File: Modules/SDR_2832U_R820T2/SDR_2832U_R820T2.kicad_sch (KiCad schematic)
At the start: 0 parts

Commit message: RTL Module Schematic
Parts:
- added C1, C2: 1u, libraries:Worthington_C_0402, symbol Device:C_Small
- added C10, C11, C12, C13, C14, C15, C16, C17, C18, C19, C20, C21, C22, C23, C24, C25, C26, C29, C30, C31, C32, C33, C52, C54, C55, C56, C57, C58, C59, C60, C63, C64, C7, C8, C9: 100n, libraries:Worthington_C_0201, symbol Device:C_Small
- added C27, C4, C5, C6, C62: 10u, libraries:Worthington_C_0402, symbol Device:C_Small
- added C28: 47u, libraries:Worthington_C_0805, symbol Device:C_Small
- added C34: 1n, ±10%, Capacitor_SMD:C_1808_4520Metric, symbol Device:C_Small
- added C37: 2u2, libraries:Worthington_C_0402_0603, symbol Device:C_Small
- added C50: 6n8, libraries:Worthington_C_0201, symbol Device:C_Small
- added C53: 330p, libraries:Worthington_C_0201, symbol Device:C_Small
- added C61: 1u, libraries:Worthington_C_0201, symbol Device:C_Small
- added D1: SM05CN-SL, Package_TO_SOT_SMD:SOT-23, symbol Power_Protection:NUP2105L
- added D10, D11, D12, D13, D9: SLZST311N10, Diode_SMD:D_SOD-882, symbol Diode:ESD9B3.3ST5G
- added D14: RB521S-30, Diode_SMD:D_SOD-523, symbol Device:D_Schottky
- added D6: RED, libraries:Worthington_LED_0402, symbol Device:LED_Filled
- added DN1: D3V3X8U9LP3810, Package_DFN_QFN:Diodes_UDFN3810-9_TYPE_B, symbol Power_Protection:D3V3X8U9LP3810
- added H1, H2, H3, H4: M2.5, MountingHole:MountingHole_2.7mm_M2.5_ISO7380_Pad, symbol Mechanical:MountingHole_Pad
- added J1: USB_C_Receptacle_USB2.0_16P, symbol Connector:USB_C_Receptacle_USB2.0_16P
- added J10, J11, J12, J8, J9: SMA, Connector_Coaxial:SMA_Molex_73251-2200_Horizontal, symbol Connector:Conn_Coaxial
- added J4, J5: 2.54 Pins, Connector_PinHeader_2.54mm:PinHeader_2x02_P2.54mm_Vertical, symbol Connector_Generic:Conn_01x04
- added J6: 2.54 Pins, Connector_PinHeader_2.54mm:PinHeader_2x04_P2.54mm_Vertical, symbol Connector_Generic:Conn_01x08
- added J7: 2.54 Sockets, Connector_PinHeader_2.54mm:PinHeader_1x03_P2.54mm_Vertical, symbol Connector_Generic:Conn_01x03
- added L1: 4u7,±20%, Inductor_SMD:L_1008_2520Metric, symbol Device:L
- added L2: 8n2, ±2%, libraries:Worthington_L_0603_RF, symbol Device:L_Small
- added L3, L4: 150n, libraries:Worthington_L_0603_RF, symbol Device:L_Small
- added Q1: GSFJ0300, Package_TO_SOT_SMD:SOT-563, symbol Transistor_FET:Q_Dual_NMOS_S1G1D2S2G2D1
- added R10, R11, R28, R29: 0, libraries:Worthington_R_0201, symbol Device:R_Small_US
- added R12, R14: 0R, libraries:Worthington_R_0201, symbol Device:R_Small_US
- added R13, R27, R47: 1M, libraries:Worthington_R_0201, symbol Device:R_Small_US
- added R15, R23, R48: 10k, libraries:Worthington_R_0201, symbol Device:R_Small_US
- added R16, R17, R18, R19, R49: 4k7, libraries:Worthington_R_0201, symbol Device:R_Small_US
- added R20: 2k8, libraries:Worthington_R_0201, symbol Device:R_Small_US
- added R21: 1k, libraries:Worthington_R_0201, symbol Device:R_Small_US
- added R22, R44: 1k8, libraries:Worthington_R_0201, symbol Device:R_Small_US
- added R25, R26, R30, R7, R8, R9: 49.9, libraries:Worthington_R_0201, symbol Device:R_Small_US
- added R50, R51: 5k1, libraries:Worthington_R_0201, symbol Device:R_Small_US
- added RN1, RN2: 4k7, libraries:RESCAXE80P320X160X70-8N, symbol Libraries:R_Network04_Split
- added S1: Breadboard 3D Model, libraries:Breadboard_400, symbol Graphic:SYM_Arrow45_Small
- added T1: DXW21BN2511NL, libraries:XFMR_ATB2012-50011-T000, symbol Transformer:0433BM15A0001
- added TP1, TP10, TP11, TP12, TP13, TP14, TP2, TP3, TP4, TP5, TP6, TP7, TP8, TP9: TestPoint, symbol Connector:TestPoint
- added U1, U2: NCV68061, Package_SO:TSOP-6_1.65x3.05mm_P0.95mm, symbol Power_Management:LM66100DCK
- added U5: RTL2832U, Package_DFN_QFN:QFN-48-1EP_6x6mm_P0.4mm_EP4.2x4.2mm_ThermalVias, symbol RTLSDR:RTL2832U
- added U6: M24C02-WMN, Package_SO:SOIC-8_3.9x4.9mm_P1.27mm, symbol Memory_EEPROM:M24C02-WMN
- added U7: AP2127K-ADJ, Package_TO_SOT_SMD:SOT-23-5, symbol Regulator_Linear:SPX3819M5-L
- added U8: LM66200, Package_TO_SOT_SMD:SOT-583-8, symbol libraries:LM66200
- added U9: R820T2, Package_DFN_QFN:QFN-24-1EP_4x4mm_P0.5mm_EP2.15x2.15mm_ThermalVias, symbol RTLSDR:R820T2
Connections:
- new net: C30.1, R26.1, R8.2
- new net: C52.2, R47.2, U9.8 (XIN/28.8MHz)
- new net: J1.B5 (CC2), R50.2
- new net: C29.1, R25.1, R7.2
- new net: Q1.2 (G), U2.2 (G)
- new net: C2.1, Q1.6 (D), U2.3 (D), U8.6 (VIN2)
- new net: C50.1, R44.1
- new net: C53.1, R44.2, U9.15 (CP)
- new net: C11.2, R10.1
- new net: R12.1, R14.1, U5.27 (ENSWREG)
- new net: C57.1, U9.10 (CLK_OUT)
- new net: C10.2, U9.12 (IF_N)
- new net: C9.2, U9.13 (IF_P)
- new net: C54.1, U9.17 (VDD_PLL)
- new net: L4.2, U9.19 (TF2N)
- new net: L3.2, U9.20 (TF2P)
- new net: L4.1, U9.21 (TF1N)
- new net: L3.1, U9.22 (TF1P)
- new net: L2.2, U9.24 (RF_IN)
- new net: C61.1, U9.4 (DET1)
- new net: C59.1, U9.5 (DET2)
- new net: R47.1, U9.9 (XOUT)
- new net: RN1.8, RN2.1 (4), U6.1 (E0)
- new net: RN1.7 (5), RN2.2, U6.2 (E1)
- new net: RN1.6, RN2.3, U6.3 (E2)
- new net: C33.1, R30.1, R9.2
- new net: C32.2, R29.1
- new net: R29.2, U5.2 (VI_N)
- new net: C31.2, R28.1
- new net: R28.2, U5.1 (VI_P)
- new net: R23.1, U8.8 (ST)
- new net: R20.1, R21.2, U7.4 (ADJ)
- new net: C37.1, L2.1
- new net: C34.1, J1.SH (SHIELD), R27.2
- new net: C1.1, Q1.3 (D), U1.3 (D), U8.3 (VIN1)
- new net: R15.1, U5.48 (R10K)
- new net: C12.2, R11.1
- new net: R11.2, U5.5 (VQ_N)
- new net: J1.A5 (CC1), R51.2
- new net: J5.2 (Pin_2), J5.4 (Pin_4), Q1.4 (S), U1.1 (S), U1.4 (EN), U1.6 (IN)
- new net: Q1.5 (G), U1.2 (G)
- new net: R13.2, U5.10 (XOUT)
- new net: C23.2, R13.1, U5.11 (XIN)
- new net: J7.2 (Pin_2), U5.15 (AGC_RF)
- new net: R10.2, U5.4 (VQ_P)
- new net: C26.1, U5.46 (VCMI)
- new net: D6.1 (K), R22.1
- new net +3V3: C14.1, C15.1, C19.1, C22.1, C25.1, C28.1, C55.1, C56.1, C58.1, C6.1, C60.1, C62.1, C64.1, D14.2 (A), D6.2 (A), R14.2, R16.1, R17.2, R18.1, R19.2, R20.2, R49.2, RN1.1 (4), RN1.2, RN1.3, RN1.4, U5.14 (VDD3V3), U5.25 (SW_VDD3V3), U5.26 (SW_VDD3V3), U5.33 (VDD3V3), U5.43 (VDDA3V3), U6.8 (VCC), U7.5 (OUT), U9.11 (+3V3), U9.18 (+3V3), U9.2 (+3V3), U9.23 (+3V3)
- new net +5V_INT: C27.1, D14.1 (K), R23.2, U7.1 (IN), U7.3 (EN), U8.2 (VOUT), U8.7 (VOUT)
- new net 28.8MHz_CLK_IN: C52.1, D11.2 (A2), J10.1 (In)
- new net 28.8MHz_CLK_OUT: C57.2, D12.2 (A2), J11.1 (In)
- new net EEPROM_SCL: R18.2, TP8.1, U5.18 (EEPROM_SCL), U6.6 (SCL)
- new net EEPROM_SDA: R16.2, TP3.1, U5.19 (EEPROM_SDA), U6.5 (SDA)
- new net GND: C1.2, C13.2, C14.2, C15.2, C16.2, C17.2, C18.2, C19.2, C2.2, C20.2, C21.2, C22.2, C24.2, C25.2, C26.2, C27.2, C28.2, C29.2, C30.2, C33.2, C34.2, C4.2, C5.2, C50.2, C53.2, C54.2, C55.2, C56.2, C58.2, C59.2, C6.2, C60.2, C61.2, C62.2, C63.2, C64.2, C7.2, C8.2, D1.3 (A), D10.1 (A1), D11.1 (A1), D12.1 (A1), D13.1 (A1), D9.1 (A1), DN1.3 (GND), H1.1, H2.1, H3.1, H4.1, J1.A1 (GND), J1.A12 (GND), J1.B1 (GND), J1.B12 (GND), J10.2 (Ext), J11.2 (Ext), J12.2 (Ext), J5.1 (Pin_1), J5.3 (Pin_3), J7.3 (Pin_3), J8.2 (Ext), J9.2 (Ext), R12.2, R15.2, R21.1, R22.2, R27.1, R50.1, R51.1, RN2.5, RN2.6, RN2.7 (5), RN2.8, T1.1, TP10.1, TP13.1, TP2.1, TP4.1, TP6.1, U1.5 (GND), U2.5 (GND), U5.3 (GNDA), U5.39 (SEGND), U5.45 (GNDA), U5.49 (EP), U5.8 (GNDPLL), U6.4 (VSS), U6.7 (~{WC}), U7.2 (GND), U8.1 (GND), U8.4 (~{ON}), U8.5 (GND), U9.16 (GND), U9.25 (EP)
- new net GPIO0: DN1.1 (Line-1), J6.1 (Pin_1), U5.37 (GPIO[0])
- new net GPIO1: DN1.9 (Line-2), J6.2 (Pin_2), U5.32 (GPIO[1])
- new net GPIO2: DN1.2 (Line-3), J6.3 (Pin_3), U5.31 (GPIO[2])
- new net GPIO3: DN1.8 (Line-4), J6.4 (Pin_4), U5.36 (GPIO[3])
- new net GPIO4: DN1.7 (Line-5), J6.5 (Pin_5), U5.30 (GPIO[4])
- new net GPIO5: DN1.4 (Line-6), J6.6 (Pin_6), U5.29 (GPIO[5])
- new net GPIO6: DN1.6 (Line-7), J6.7 (Pin_7), U5.22 (GPIO[6])
- new net GPIO7: DN1.5 (Line-8), J6.8 (Pin_8), U5.21 (GPIO[7])
- new net IF_AGC_IN: C63.1, R48.1, U9.14 (IF_AGC)
- new net IF_AGC_OUT: J7.1 (Pin_1), R48.2, R49.1, U5.13 (AGC_IF)
- new net IF_I+: C31.1, C9.1, R26.2, R30.2, TP9.1
- new net IF_I-: C10.1, C32.1, R8.1, R9.1, TP11.1
- new net IF_Q+: C11.1, R25.2, T1.3, TP14.1
- new net IF_Q-: C12.1, R7.1, T1.4, TP12.1
- new net RF_IN_HIGH: C37.2, D9.2 (A2), J8.1 (In)
- new net RF_IN_LOW: D10.2 (A2), J9.1 (In), T1.2
- new net RTL_1V2: C13.1, C16.1, C17.1, C18.1, C20.1, C21.1, C24.1, C4.1, C5.1, C7.1, C8.1, L1.2, TP1.1, U5.12 (VDD1V2), U5.20 (VDD1V2), U5.23 (FB), U5.28 (VDD1V2), U5.34 (VDD1V2), U5.42 (UVDDA1V2), U5.44 (VDDA1V2), U5.47 (VDDA1V2), U5.7 (VDDPLL)
- new net RTL_1V2_OUT: L1.1, U5.24 (1V2_REG_OUT)
- new net RTL_CLK_IN: C23.1, D13.2 (A2), J12.1 (In)
- new net TUNER_SCL: R19.1, TP5.1, U5.16 (TUNER_SCL), U9.6 (SCL)
- new net TUNER_SDA: R17.1, TP7.1, U5.17 (TUNER_SDA), U9.7 (SDA)
- new net USB_SDR_D+: D1.2 (K), J1.A6 (D+), J1.B6 (D+), U5.40 (USB_DP)
- new net USB_SDR_D-: D1.1 (K), J1.A7 (D-), J1.B7 (D-), U5.41 (USB_DM)
- new net VUSB: J1.A4 (VBUS), J1.A9 (VBUS), J1.B4 (VBUS), J1.B9 (VBUS), Q1.1 (S), U2.1 (S), U2.4 (EN), U2.6 (IN)
- no-connect marks 0 -> 9
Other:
- note added: "/* * GPIO 0 .. 7 correspond to RTL2832U's pins as follows: * Pin information from http://lea.hamradio.si/~s57uuu/mischam/rtlsdr/ports.html * * GPIO0 (=pin 37): BiasT for RTL-SDR.com V3 * GPIO1 (=pin 32): usually free - on RTL-SDR.com V3's Expansion Ports * GPIO2 (=pin 31): usually free - on RTL-SDR.com V3's Expansion Ports * GPIO3 (=pin 36): usually free * GPIO4 (=pin 30): RESET for Tuners FC2580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"
- note added: "3V3 LDO"
- note added: "Allows PCB to survive being placed onto breadboard in wrong orientation"
- note added: "Input Power Selector"
- note added: "LINK: RTL-SDR GPIO Mapping (Line 612)"
- note added: "Reverse Polarity Protection Reverse Current Protection"
- note added: "Used to oriente PCB on breadboard"

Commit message: Placed footprints on PCB
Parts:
- added D10, D11, D12, D13, D14, D15, D16, D9: AMBER, libraries:Worthington_LED_0402, symbol Device:LED_Filled
- added RN3, RN4: 1k, libraries:RESCAXE80P320X160X70-8N, symbol Libraries:R_Network04_Split
- J5: renamed from J1; footprint (none) -> Connector_USB:USB_C_Receptacle_Amphenol_124019772112A
- TP1: renamed from TP9; footprint (none) -> TestPoint:TestPoint_Keystone_5000-5004_Miniature
- TP10: renamed from TP1; footprint (none) -> TestPoint:TestPoint_Keystone_5000-5004_Miniature
- TP11: renamed from TP2; footprint (none) -> TestPoint:TestPoint_Keystone_5000-5004_Miniature
- TP12: renamed from TP3; footprint (none) -> TestPoint:TestPoint_Keystone_5000-5004_Miniature
- TP13: renamed from TP4; footprint (none) -> TestPoint:TestPoint_Keystone_5000-5004_Miniature
- TP14: renamed from TP8; footprint (none) -> TestPoint:TestPoint_Keystone_5000-5004_Miniature
- TP2: renamed from TP10; footprint (none) -> TestPoint:TestPoint_Keystone_5000-5004_Miniature
- TP3: renamed from TP5; footprint (none) -> TestPoint:TestPoint_Keystone_5000-5004_Miniature
- TP4: renamed from TP11; footprint (none) -> TestPoint:TestPoint_Keystone_5000-5004_Miniature
- TP5: renamed from TP6; footprint (none) -> TestPoint:TestPoint_Keystone_5000-5004_Miniature
- TP6: renamed from TP7; footprint (none) -> TestPoint:TestPoint_Keystone_5000-5004_Miniature
- TP7: renamed from TP12; footprint (none) -> TestPoint:TestPoint_Keystone_5000-5004_Miniature
- TP8: renamed from TP13; footprint (none) -> TestPoint:TestPoint_Keystone_5000-5004_Miniature
- TP9: renamed from TP14; footprint (none) -> TestPoint:TestPoint_Keystone_5000-5004_Miniature
- renumbered C34 to C1, C56 to C10, C57 to C11, C59 to C12, C9 to C13, C10 to C14, C61 to C15, C27 to C16, C58 to C17, C63 to C18, C60 to C19, C37 to C2, C33 to C20, C62 to C21, C64 to C22, C28 to C23, C4 to C24, C5 to C25, C6 to C26, C7 to C27, C13 to C28, C8 to C29, C50 to C3, C29 to C31, C14 to C32, C16 to C33, C17 to C34, C18 to C35, C19 to C36, C31 to C37, C32 to C38, C11 to C39, C2 to C4, C12 to C40, C20 to C41, C21 to C42, C22 to C43, C23 to C44, C24 to C45, C25 to C46, C15 to C47, C26 to C48, C1 to C5, C52 to C6, C53 to C7, C54 to C8, C55 to C9, D9 to D1, D11 to D2, D1 to D3, D14 to D4, D12 to D5, D10 to D6, D6 to D7, D13 to D8, J4 to J1, J6 to J10, J5 to J2, J8 to J3, J10 to J4, J11 to J6, J9 to J7, J12 to J8, J7 to J9, L2 to L1, L3 to L2, L4 to L3, L1 to L4, R27 to R1, R49 to R10, R20 to R11, R21 to R12, R22 to R13, R26 to R14, R8 to R15, R25 to R16, R7 to R17, R28 to R18, R29 to R19, R44 to R2, R10 to R20, R11 to R21, R12 to R22, R13 to R23, R14 to R24, R15 to R25, R17 to R26, R16 to R27, R19 to R28, R18 to R29, R47 to R3, R50 to R4, R51 to R5, R23 to R6, R30 to R7, R9 to R8, R48 to R9, U2 to U1, U1 to U2, U8 to U3, U9 to U4, U7 to U5, U5 to U6, U6 to U7
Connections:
- net GND: now also RN3.5, RN3.6, RN3.7 (5), RN3.8, RN4.5, RN4.6, RN4.7 (5), RN4.8
- net GPIO7: now also D10.2 (A), D11.2 (A), D12.2 (A), D13.2 (A), D14.2 (A), D15.2 (A), D16.2 (A), D9.2 (A)
- new net: D16.1 (K), RN4.4
- new net: D11.1 (K), RN3.3
- new net: D15.1 (K), RN4.3
- new net: D10.1 (K), RN3.2
- new net: D12.1 (K), RN3.4
- new net: D13.1 (K), RN4.1 (4)
- new net: D14.1 (K), RN4.2
- new net: D9.1 (K), RN3.1 (4)
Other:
- moved on the sheet: DN1, J10

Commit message: PCB progress
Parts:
- added C49, C50, C51: 100n, libraries:Worthington_C_Narrow_0201, symbol Device:C_Small
- added C52: 47u, libraries:Worthington_C_Narrow_0603, symbol Device:C_Small
- C10, C11, C12, C13, C14, C15, C17, C18, C19, C20, C22, C27, C28, C29, C3, C30, C31, C32, C33, C34, C35, C36, C37, C38, C39, C40, C41, C42, C43, C44, C45, C46, C47, C48, C6, C7, C8, C9: footprint libraries:Worthington_C_0201 -> libraries:Worthington_C_Narrow_0201
- C16, C21, C24, C25, C26, C4, C5: footprint libraries:Worthington_C_0402 -> libraries:Worthington_C_Narrow_0402
- C2: footprint libraries:Worthington_C_0402_0603 -> libraries:Worthington_C_Narrow_0402_0603
- J3, J4, J6, J7, J8: footprint Connector_Coaxial:SMA_Molex_73251-2200_Horizontal -> Connector_Coaxial:SMA_Amphenol_132289_EdgeMount
- J5: footprint Connector_USB:USB_C_Receptacle_Amphenol_124019772112A -> Connector_USB:USB_C_Receptacle_GCT_USB4105-xx-A_16P_TopMnt_Horizontal
- L1, L2, L3: footprint libraries:Worthington_L_0603_RF -> libraries:Worthington_L_Narrow_0603_RF
- R1, R10, R11, R12, R13, R14, R15, R16, R17, R18, R19, R2, R20, R21, R22, R23, R24, R25, R26, R27, R28, R29, R3, R4, R5, R6, R7, R8, R9: footprint libraries:Worthington_R_0201 -> libraries:Worthington_R_Narrow_0201
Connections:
- net GND: now also T1.2, C49.2, C50.2, C51.2, C52.2; no longer T1.1
- net IF_Q+: now also T1.4; no longer T1.3
- net IF_Q-: now also T1.3; no longer T1.4
- net RF_IN_LOW: now also T1.1; no longer T1.2
- net RTL_1V2: now also C52.1
- net at C30.1, R14.1, R15.2: now also C49.1
- net at C31.1, R16.1, R17.2: now also C50.1
- net at C20.1, R7.1, R8.2: now also C51.1
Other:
- moved on the sheet: C20, C30, C31, C37, C38, C39, C40, D2, D5, D6, J7, R14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

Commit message: PCB progress
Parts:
- removed DN1: D3V3X8U9LP3810, Package_DFN_QFN:Diodes_UDFN3810-9_TYPE_B, symbol Power_Protection:D3V3X8U9LP3810
- removed TP1, TP11, TP2, TP4, TP7, TP8, TP9: TestPoint, TestPoint:TestPoint_Keystone_5000-5004_Miniature, symbol Connector:TestPoint
- added C53: 100n, libraries:Worthington_C_Narrow_0201, symbol Device:C_Small
- added D17, D18: PUSB3FR4, Package_DFN_QFN:Diodes_UDFN-10_1x2.5mm_P0.5mm, symbol Power_Protection:ESDA14V2SC5
- added J11: 2.54 Pins, Connector_PinHeader_2.54mm:PinHeader_1x04_P2.54mm_Vertical, symbol Connector_Generic:Conn_01x04
- D3: value SM05CN-SL -> DF3A6.8LFV,L3F; footprint Package_TO_SOT_SMD:SOT-23 -> Package_TO_SOT_SMD:SOT-723
- J10: footprint Connector_PinHeader_2.54mm:PinHeader_2x04_P2.54mm_Vertical -> Connector_PinHeader_2.54mm:PinHeader_1x04_P2.54mm_Vertical; symbol Connector_Generic:Conn_01x08 -> Connector_Generic:Conn_01x04
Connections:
- net +3V3: now also C53.1
- net GND: now also U1.1 (NC), U1.2 (GND), U2.1 (NC), U2.2 (GND), C53.2, D17.3 (A), D17.8 (A), D18.3 (A), D18.8 (A); no longer U1.5 (GND), U2.5 (GND)
- net GPIO0: now also D16.2 (A), D17.5 (K)
- net GPIO1: now also D15.2 (A), D17.4 (K)
- net GPIO2: now also D14.2 (A), D17.2 (K)
- net GPIO3: now also D13.2 (A), D17.1 (K)
- net GPIO4: now also D12.2 (A), D18.5 (K), J11.1 (Pin_1); no longer J10.5 (Pin_5)
- net GPIO5: now also D11.2 (A), D18.4 (K), J11.2 (Pin_2); no longer J10.6 (Pin_6)
- net GPIO6: now also D10.2 (A), D18.2 (K), J11.3 (Pin_3); no longer J10.7 (Pin_7)
- net GPIO7: now also D18.1 (K), J11.4 (Pin_4); no longer D10.2 (A), D11.2 (A), D12.2 (A), D13.2 (A), D14.2 (A), D15.2 (A), D16.2 (A), J10.8 (Pin_8)
- net VUSB: now also U1.3 (EN); no longer U1.1 (S), U1.4 (EN)
- net at Q1.2 (G): now also U1.5 (G); no longer U1.2 (G)
- net at C4.1, Q1.6 (D), U3.6 (VIN2): now also U1.4 (D); no longer U1.3 (D)
- net at RN4.4: now also D13.1 (K); no longer D16.1 (K)
- net at RN3.3: now also D10.1 (K); no longer D11.1 (K)
- net at RN1.7 (5), RN2.2: now also U7.3 (E2); no longer U7.2 (E1)
- net at RN1.6, RN2.3: now also U7.2 (E1); no longer U7.3 (E2)
- net at D15.1 (K): now also RN4.2; no longer RN4.3
- net at RN2.4: now also RN1.5, U7.1 (E0)
- net at RN3.2: now also D11.1 (K); no longer D10.1 (K)
- net at C5.1, Q1.3 (D), U3.3 (VIN1): now also U2.4 (D); no longer U2.3 (D)
- net at RN3.4: now also D9.1 (K); no longer D12.1 (K)
- net at RN4.1 (4): now also D16.1 (K); no longer D13.1 (K)
- net at D14.1 (K): now also RN4.3; no longer RN4.2
- net at J2.2 (Pin_2), J2.4 (Pin_4), Q1.4 (S)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: now also U2.3 (EN); no longer U2.1 (S), U2.4 (EN)
- net at Q1.5 (G): now also U2.5 (G); no longer U2.2 (G)
- net at RN3.1 (4): now also D12.1 (K); no longer D9.1 (K)
- new net: D17.10 (A), D17.6 (A), D17.7 (A), D17.9 (A)
- new net: D18.10 (A), D18.6 (A), D18.7 (A), D18.9 (A)
- now unconnected: RN1.8, RN2.1 (4)
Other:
- moved on the sheet: D10, D11, D12, D13, D14, D15, D16, D9, RN1A, RN2A, RN3A, RN4A

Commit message: PCB Layout Completed
Now I need to do the silkscreen stuffs...
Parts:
- added R30, R31: 33?, libraries:Worthington_R_Narrow_0201, symbol Device:R_Small_US
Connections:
- net +3V3: now also R13.1; no longer D7.2 (A)
- net GND: now also D7.1 (K); no longer R13.2
- net USB_SDR_D+: now also R30.1; no longer U6.40 (USB_DP)
- net USB_SDR_D-: now also R31.2; no longer U6.41 (USB_DM)
- new net: R31.1, U6.41 (USB_DM)
- new net: R30.2, U6.40 (USB_DP)
- new net: D7.2 (A), R13.2
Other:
- moved on the sheet: C24, C52, D7, R13

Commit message: Added termination resistors to CLK lines
And did some silkscreen tweaks
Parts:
- added R32, R33, R36, R37: 10k, libraries:Worthington_R_Narrow_0201, symbol Device:R_Small_US
- added R34, R35: 220, libraries:Worthington_R_Narrow_0201, symbol Device:R_Small_US
- added TP4, TP7: TestPoint, TestPoint:TestPoint_Keystone_5000-5004_Miniature, symbol Connector:TestPoint
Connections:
- net +3V3: now also R32.2, R36.2
- net +5V_INT: now also TP4.1
- net GND: now also R33.1, R37.1, TP7.1
- net IF_I+: no longer R7.2
- net IF_I-: no longer R8.1
- net at C6.2, R3.2, U4.8 (XIN/28.8MHz): now also R32.1, R33.2
- net at U4.12 (IF_N): now also R35.1; no longer C14.2
- net at U4.13 (IF_P): now also R34.1; no longer C13.2
- net at C44.2, R23.1, U6.11 (XIN): now also R36.1, R37.2
- new net: C13.2, R34.2, R7.2
- new net: C14.2, R35.2, R8.1
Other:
- note added: "+0V to +3V3"
- note added: "2.0V_{pp} Triangle"
- note added: "2.45V_{pp} MAX"
- moved on the sheet: C13, C14, C37, C44, C6, D2, J4

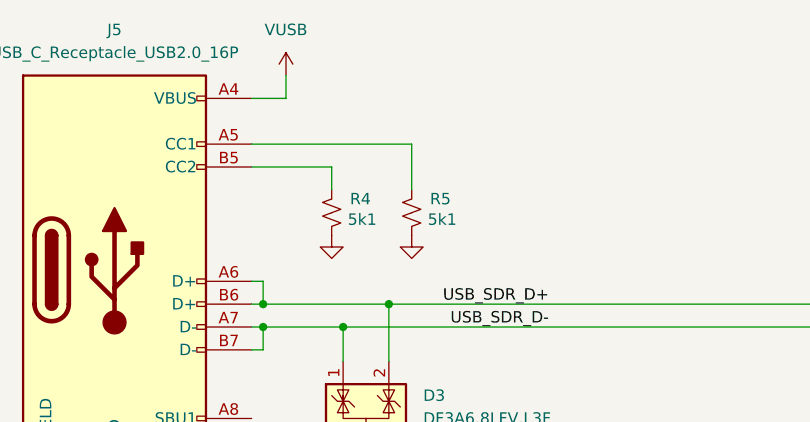
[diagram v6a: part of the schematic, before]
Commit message: Added input power snubber
Just in case :P
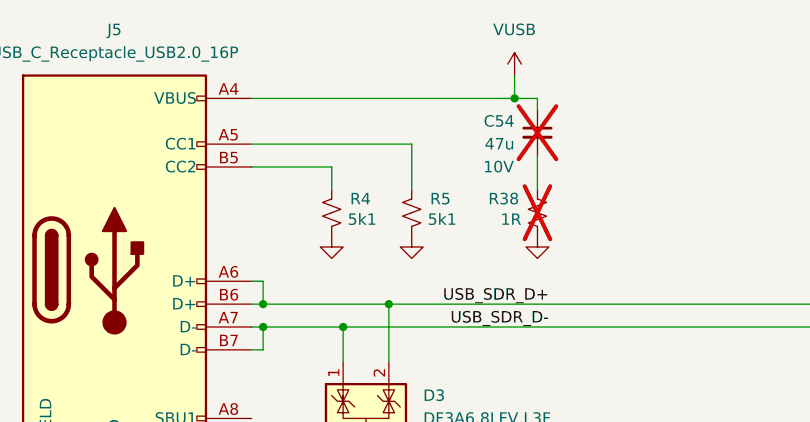
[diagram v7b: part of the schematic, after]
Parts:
- added C54: 47u, libraries:Worthington_C_0805, symbol Device:C_Small
- added R38: 1R, Resistor_SMD:R_0805_2012Metric, symbol Device:R_Small_US
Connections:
- net GND: now also R38.1
- net VUSB: now also C54.1
- new net: C54.2, R38.2
